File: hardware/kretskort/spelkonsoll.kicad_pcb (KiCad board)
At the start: 2 copper layers, 176.6 x 56.6 mm, 19 parts, among them J1 USB_C_Receptacle_USB2.0, SW1 SW_Push, SW10 SW_Push, SW11 SW_Push, SW12 SW_Push, SW2 SW_Push, SW3 SW_Push, SW4 SW_Push, SW5 SW_Push, SW6 SW_Push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

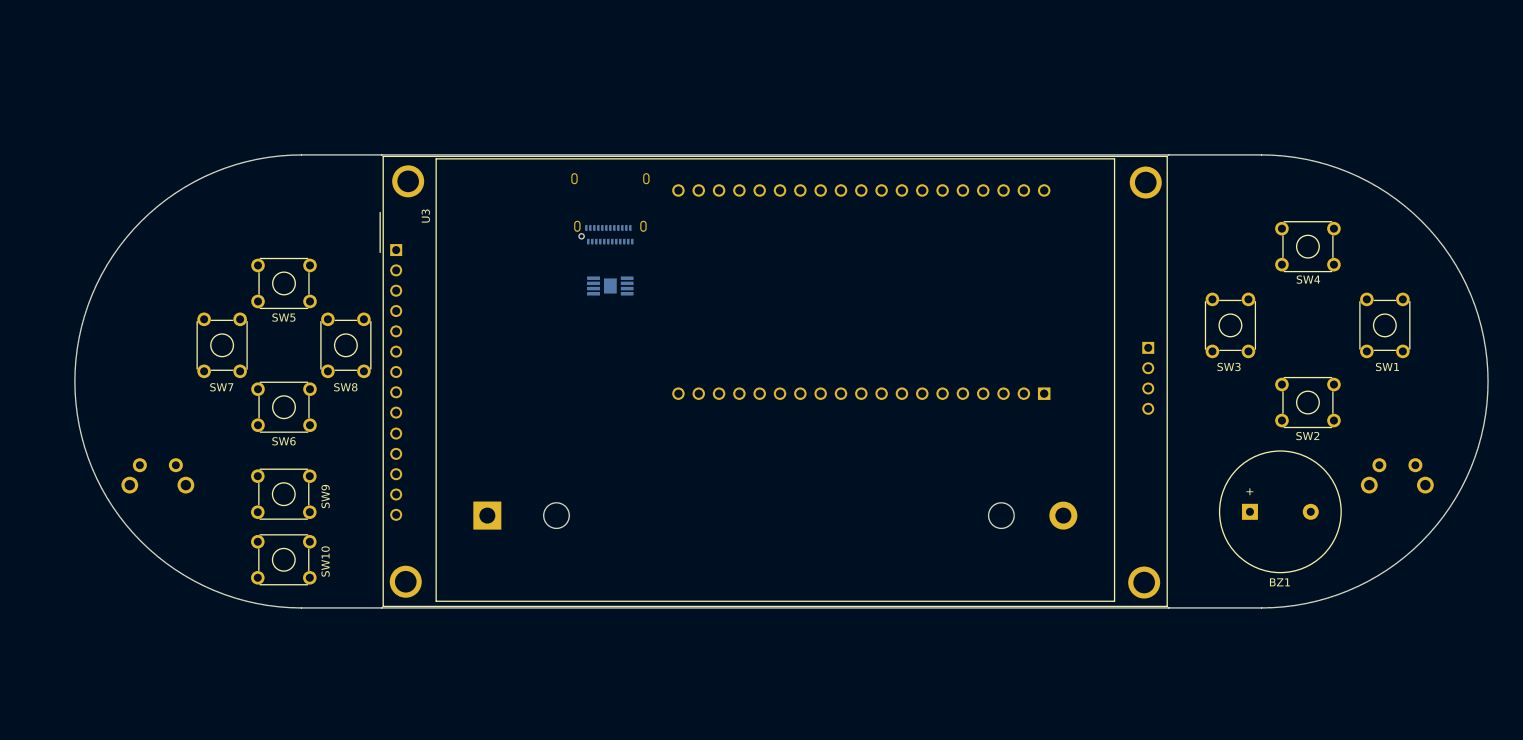
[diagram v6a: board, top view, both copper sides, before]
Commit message: modified buttons to maybe work
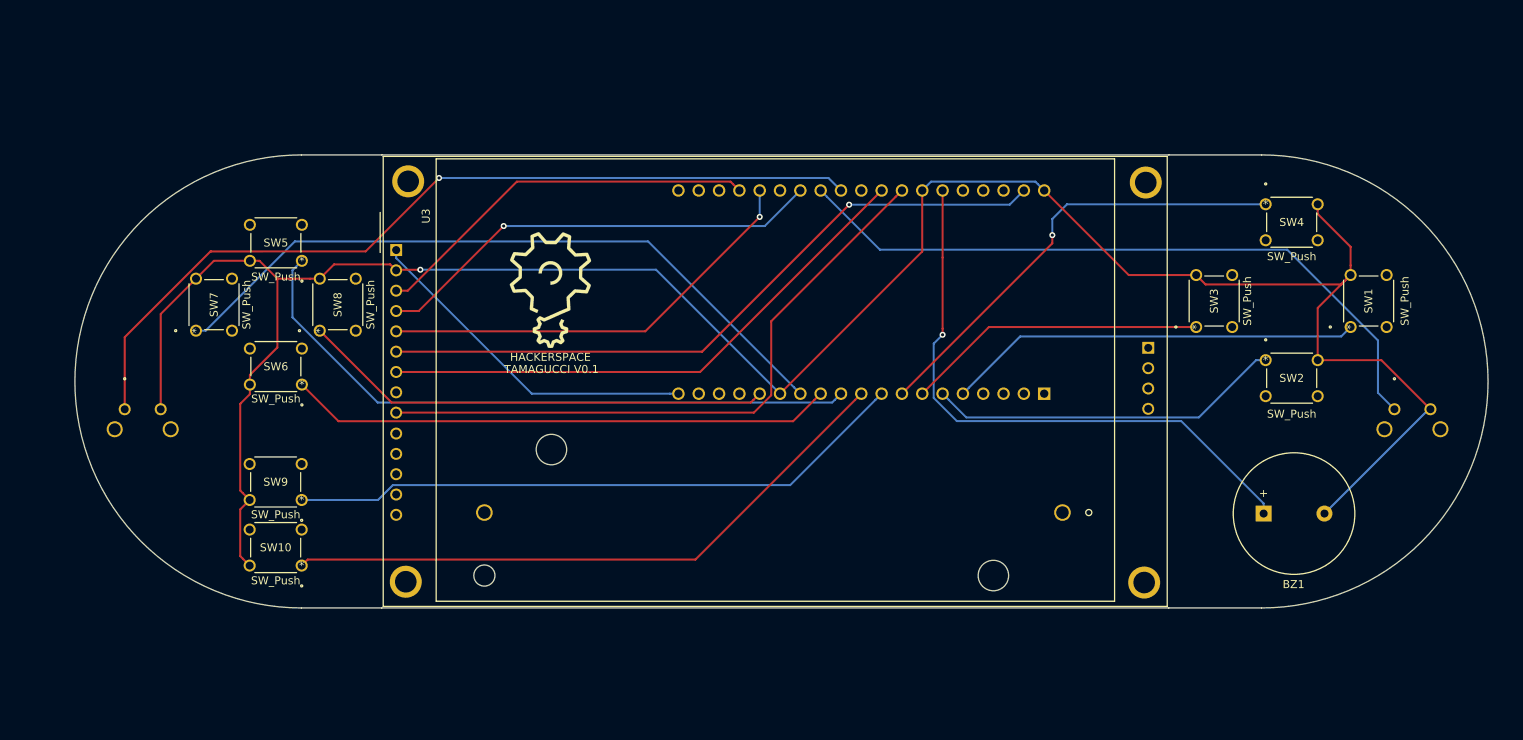
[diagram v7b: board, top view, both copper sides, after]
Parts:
- removed the G*** at (109.2, 92.7)
- removed J1: USB_C_Receptacle_USB2.0, Connector_USB:USB_C_Receptacle_Amphenol_12401610E4-2A
- removed U1: BQ24202DGN, Strøm:BQ24202DGN
- added G***: LOGO, kretskort:hs_logo, F.Cu at (117.3, 86.1)
- added G***: LOGO, kretskort:hs_logo, B.Cu at (117.3, 86.1)
- BT1: footprint Battery:BatteryHolder_MPD_BH-18650-PC2 -> footprints:18650holder
- SW1, SW10, SW2, SW3, SW4, SW5, SW6, SW7, SW8, SW9: footprint Button_Switch_THT:SW_TH_Tactile_Omron_B3F-10xx -> footprints:B3F1052
- SW11, SW12: footprint Button_Switch_THT:SW_Tactile_SPST_Angled_PTS645Vx83-2LFS -> footprints:B3F-3152
- moved SW11 9.48 mm to (64.1, 101.0), turned to 0 degrees
- moved SW12 7.47 mm to (222.8, 101.0), turned to 0 degrees
- moved SW7 5.18 mm to (73.0, 91.2)
- moved SW5 5.18 mm to (86.3, 82.5)
- moved SW6 5.18 mm to (86.3, 97.9)
- moved SW8 5.18 mm to (88.5, 91.2)
- moved SW1 3.66 mm to (217.4, 90.7)
- moved SW2 3.66 mm to (206.8, 94.9)
- moved SW4 3.66 mm to (206.8, 75.4)
- moved SW3 3.66 mm to (198.1, 90.7)
- moved SW10 1.83 mm to (86.3, 120.5)
- moved SW9 1.83 mm to (86.3, 112.3)
- moved BZ1 1.72 mm to (206.5, 114.0)
- moved BT1 0.53 mm to (109.1, 113.9), turned to 180 degrees
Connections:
- U3 pad 8: +5V -> Net-(U3-Pad8)
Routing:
- net GND: track 0.00 -> 290.5 mm, vias 0 -> 1
- net BTN_BUMPER_L: track 0.00 -> 107.4 mm, vias 0 -> 1
- net BTN_DP_LEFT: track 0.00 -> 88.0 mm
- net BTN_BUMPER_R: track 0.00 -> 86.9 mm
- net MOSI: track 0.00 -> 86.8 mm, vias 0 -> 1
- net BTN_DP_UP: track 0.00 -> 81.0 mm
- net MISO: track 0.00 -> 80.1 mm
- net BTN_SELECT: track 0.00 -> 78.9 mm
- net BTN_START: track 0.00 -> 78.0 mm
- net BUZZER: track 0.00 -> 74.4 mm, vias 0 -> 1
- net SCK: track 0.00 -> 70.1 mm
- net BTN_DP_DOWN: track 0.00 -> 68.2 mm
- net BTN_DP_RIGHT: track 0.00 -> 59.2 mm
- net BTN_Y: track 0.00 -> 57.1 mm, vias 0 -> 1
- net RESET: track 0.00 -> 56.8 mm, vias 0 -> 1
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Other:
- board text added: "TAMAGUCCI V0.1"

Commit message: lol glemte å lagre igjen
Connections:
- SW1 pad 2: GND -> +5V
- SW10 pad 2: GND -> +5V
- SW11 pad 2: GND -> +5V
- SW12 pad 2: GND -> +5V
- SW2 pad 2: GND -> +5V
- SW3 pad 2: GND -> +5V
- SW4 pad 2: GND -> +5V
- SW5 pad 2: GND -> +5V
- SW6 pad 2: GND -> +5V
- SW7 pad 2: GND -> +5V
- SW8 pad 2: GND -> +5V
- SW9 pad 2: GND -> +5V
- U2 pad 10: BTN_SELECT -> BTN_START
- U2 pad 5: BTN_A -> BTN_B
- U2 pad 6: BTN_B -> BTN_A
- U2 pad 9: BTN_START -> BTN_SELECT
- U3 pad 8: Net-(U3-Pad8) -> +5V
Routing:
- net +5V: track 43.3 -> 266.0 mm
- net GND: track 290.5 -> 164.6 mm, vias 1 -> 0
- net BUZZER: track 74.4 -> 58.2 mm, vias 1 -> 0
- net DC\RS: track 54.7 -> 61.7 mm, vias 1 -> 0
- net BTN_DP_LEFT: track 88.0 -> 82.0 mm
- net BTN_BUMPER_R: track 86.9 -> 92.3 mm
- net MISO: track 80.1 -> 74.7 mm
- net BTN_B: track 44.6 -> 39.6 mm
- net BTN_DP_UP: track 81.0 -> 76.3 mm
- net BTN_DP_RIGHT: track 59.2 -> 62.4 mm
- net BTN_SELECT: track 78.9 -> 81.4 mm
- net BTN_A: track 51.9 -> 54.5 mm
- net BTN_START: track 78.0 -> 76.1 mm
- net BTN_BUMPER_L: track 107.4 -> 106.1 mm, vias 1 -> 0
- net CS: track 49.0 -> 48.1 mm
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- added copper zone on B.Cu, net GND
- added copper zone on F.Cu, net GND
